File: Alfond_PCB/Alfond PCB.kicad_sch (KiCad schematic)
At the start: 33 parts, among them J1 USB_B_Micro, J2 Micro_SD_Card, U1 AMS1117-3.3, U2 DS18B20, U3 AM2302, U4 STM32U535VCT6, Y1 16MHz

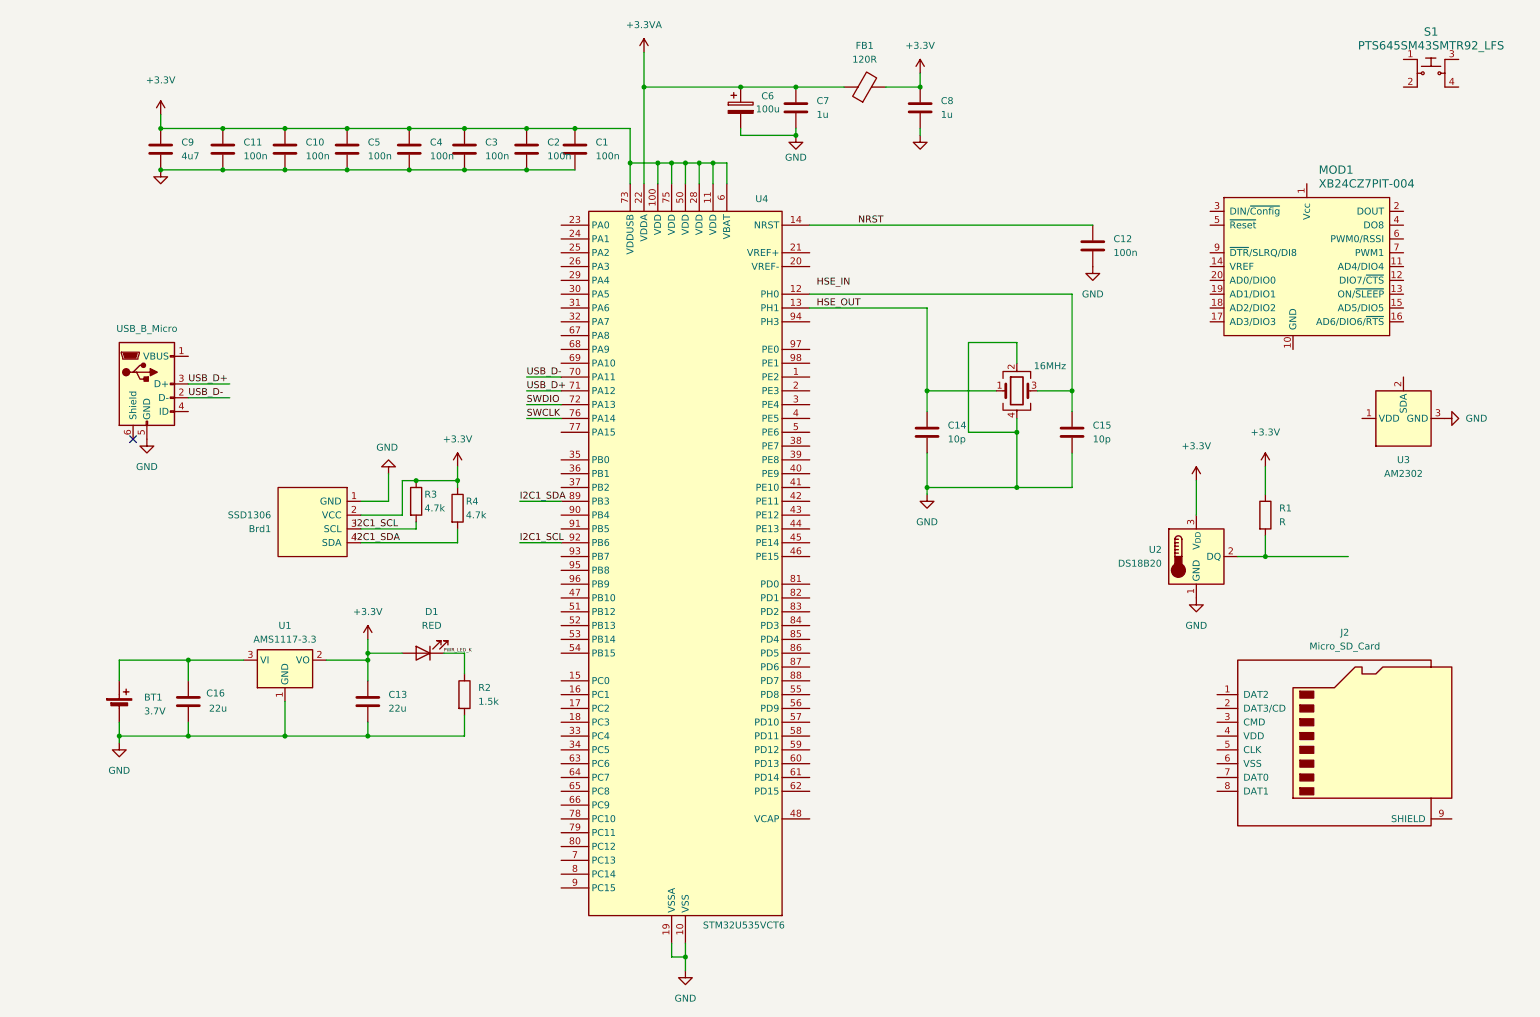
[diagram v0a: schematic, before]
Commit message: Removed stm32ide files because they were causing errors
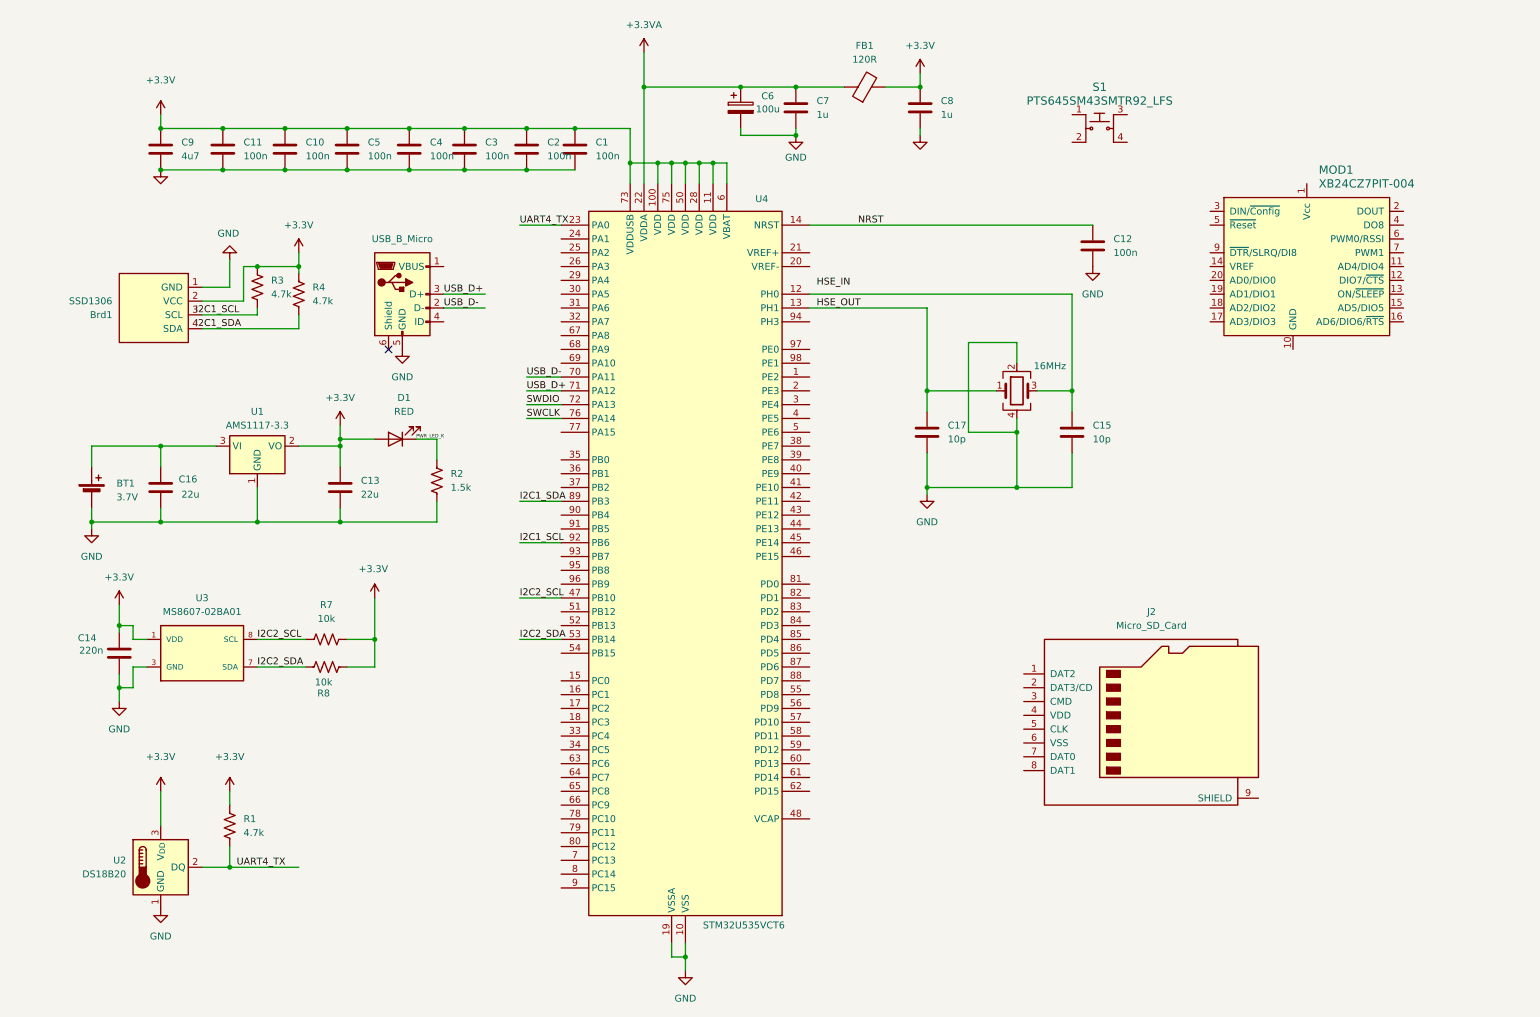
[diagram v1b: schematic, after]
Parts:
- removed R1: R, symbol Device:R
- removed R2: 1.5k, symbol Device:R
- removed R3, R4: 4.7k, symbol Device:R
- removed U3: AM2302, Sensor:ASAIR_AM2302_P2.54mm_Vertical, symbol Sensor:AM2302
- added C17: 10p, symbol Device:C
- added R1, R3, R4: 4.7k, symbol Device:R_US
- added R2: 1.5k, symbol Device:R_US
- added R7, R8: 10k, symbol Device:R_US
- added U3: MS8607-02BA01, MS8607-02BA01:MS8607-02BA01, symbol MS8607-02BA01:MS8607-02BA01
- C14: value 10p -> 220n
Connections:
- net +3.3V: now also C14.1, R1.1, R3.1, R4.1, R7.2, R8.2, U3.1 (VDD)
- net GND: now also C17.2, R2.2, U3.3 (GND)
- net HSE_OUT: now also C17.1; no longer C14.1
- net PWR_LED_K: now also R2.1
- net UART4_TX: now reaches U2.2 (DQ)
- net UART4_TX: now also U4.23 (PA0), R1.2
- net at Brd1.4 (SDA): now also R4.2
- net at Brd1.3 (SCL): now also R3.2
- net I2C2_SCL: now reaches U4.47 (PB10)
- net I2C2_SCL: now also R7.1, U3.8 (SCL)
- net I2C2_SDA: now reaches U4.53 (PB14)
- net I2C2_SDA: now also R8.1, U3.7 (SDA)
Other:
- moved on the sheet: BT1, Brd1, C13, C16, D1, J2, S1, U1, U2

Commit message: removed stm32ide files
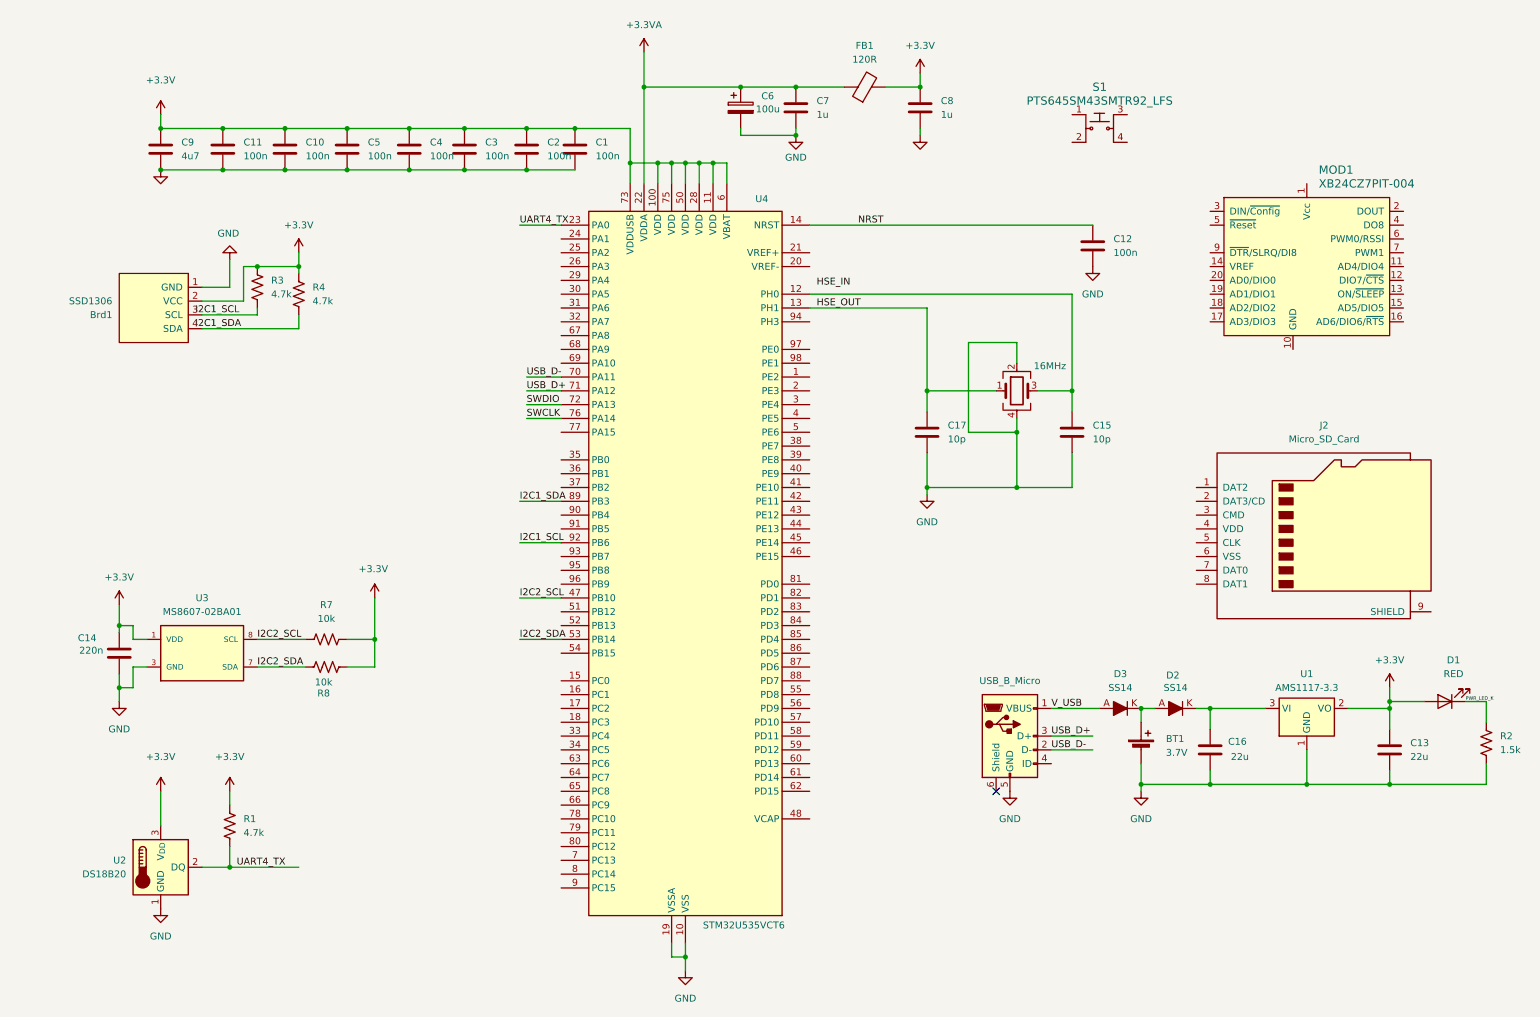
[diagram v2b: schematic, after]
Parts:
- added D2, D3: SS14, digikey-footprints:DO-214AC, symbol dk_Diodes-Rectifiers-Single:SS14
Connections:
- net V_USB: now reaches J1.1 (VBUS)
- net V_USB: now also D3.A
- net at C16.1, U1.3 (VI): now also D2.K; no longer BT1.1 (+)
- new net: BT1.1 (+), D2.A, D3.K
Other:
- moved on the sheet: BT1, C13, C16, D1, J2, R2, U1

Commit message: Updated schematic with xbee, sd card slot and button
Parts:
- removed J2: Micro_SD_Card, symbol Connector:Micro_SD_Card
- removed S1: PTS645SM43SMTR92_LFS, digikey-footprints:Switch_Tactile_SMD_6x6mm_PTS645, symbol dk_Tactile-Switches:PTS645SM43SMTR92_LFS
- added C18: 0.1u, symbol Device:C
- added D4: RED, symbol Device:LED
- added J3: Micro_SD_Card_Det_Hirose_DM3AT, symbol Connector:Micro_SD_Card_Det_Hirose_DM3AT
- added R5: 1.5k, symbol Device:R_US
- added R6: 1k, symbol Device:R_US
- added R9: 10k, symbol Device:R_US
- added S2: PTS645SM43SMTR92_LFS, digikey-footprints:Switch_Tactile_SMD_6x6mm_PTS645, symbol dk_Tactile-Switches:PTS645SM43SMTR92_LFS
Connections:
- net +3.3VA is gone; now on net +3.3V: C6.1, C7.1, FB1.1, U4.22 (VDDA)
- net +3.3V: now also MOD1.1 (Vcc), J3.4 (VDD), R9.1
- net GND: now also C1.2, C10.2, C11.2, C2.2, C3.2, C4.2, C5.2, C9.2, MOD1.10 (GND), C18.2, J3.11 (SHIELD), J3.6 (VSS), R5.2, S2.1, S2.2
- net HSE_IN: now also C15.1, U4.12 (PH0), Y1.3
- net I2C1_SCL: now also Brd1.3 (SCL), R3.2
- net I2C1_SDA: now also Brd1.4 (SDA), R4.2
- net PWR_LED_K: now also D4.1 (K), R5.1
- net at MOD1.13 (ON/~{SLEEP}): now also D4.2 (A)
- net UART5_RX: now reaches MOD1.2 (DOUT)
- net UART5_RX: now also U4.83 (PD2)
- net UART5_TX: now reaches MOD1.3 (DIN/~{Config})
- net UART5_TX: now also U4.80 (PC12)
- net GPIO_SLEEP_XBEE: now reaches MOD1.9 (~{DTR}/SLRQ/DI8)
- net GPIO_SLEEP_XBEE: now also U4.82 (PD1)
- net SPI2_MOSI: now reaches U4.16 (PC1)
- net SPI2_MOSI: now also J3.3 (CMD)
- net SPI2_MISO: now reaches U4.17 (PC2)
- net SPI2_MISO: now also J3.7 (DAT0)
- net SPI2_SCK: now reaches U4.52 (PB13)
- net SPI2_SCK: now also J3.5 (CLK)
- net GPIO_SPI_CS: now reaches U4.69 (PA10)
- net GPIO_SPI_CS: now also J3.2 (DAT3/CD)
- new net: R6.1, S2.3, S2.4
- new net GPIO_INPUT_Button: C18.1, R6.2, R9.2
- no-connect marks 1 -> 88
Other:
- moved on the sheet: BT1, C12, C13, C14, C16, D1, D2, D3, MOD1, R1, R2, R7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

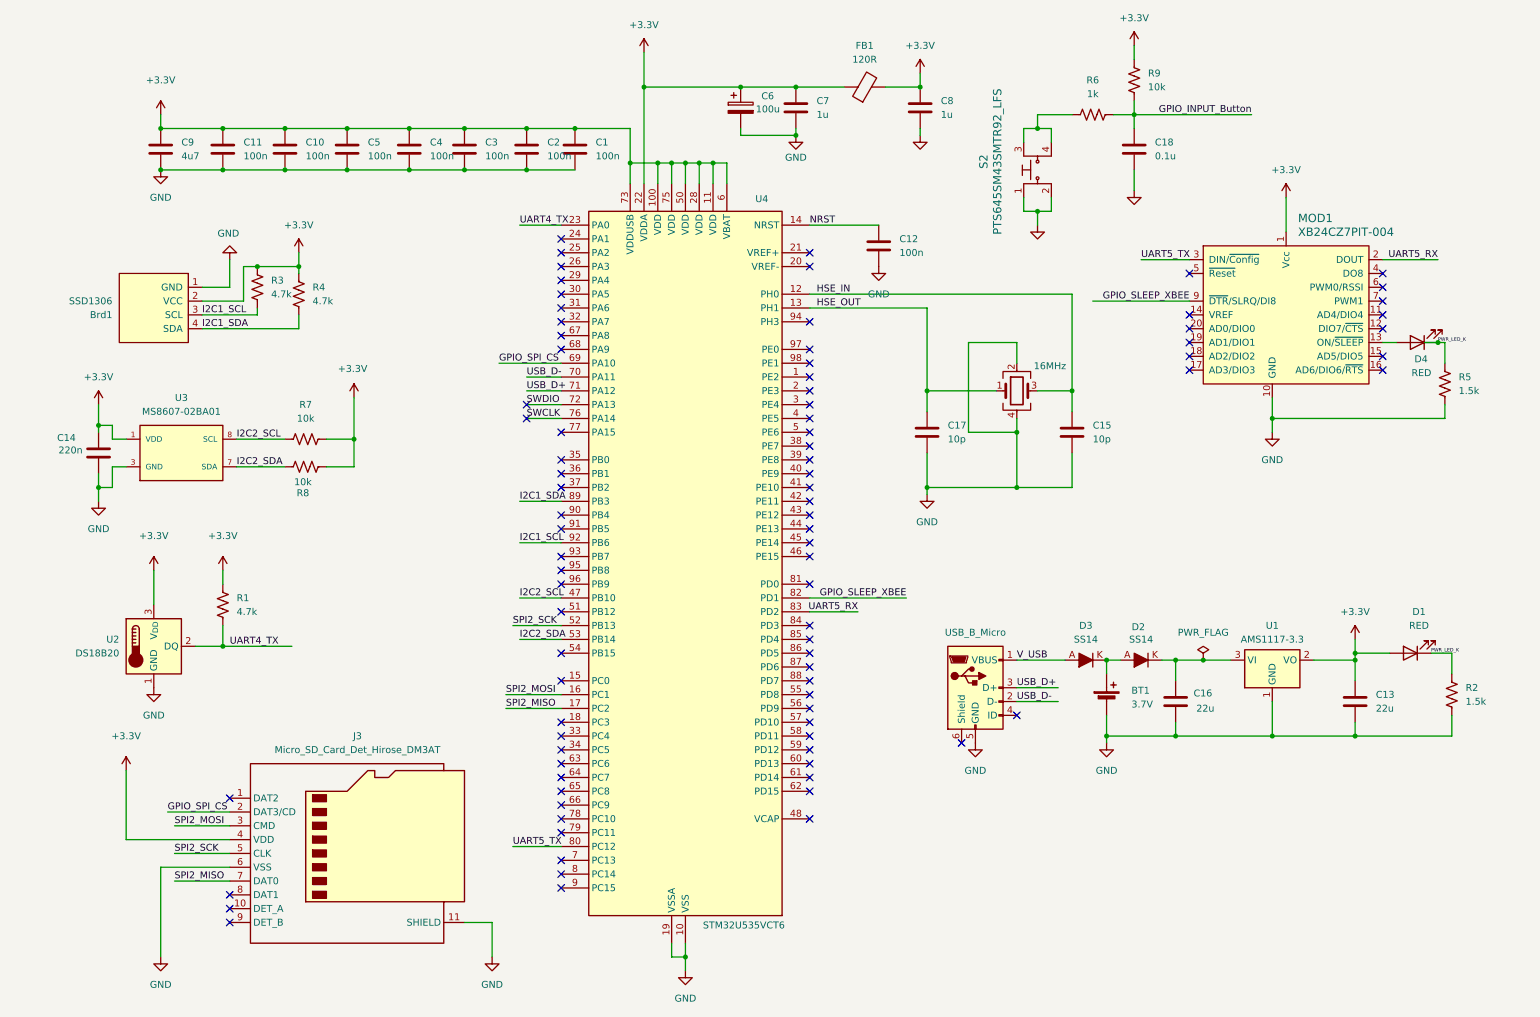
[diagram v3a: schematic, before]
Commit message: added footprints to the symbols
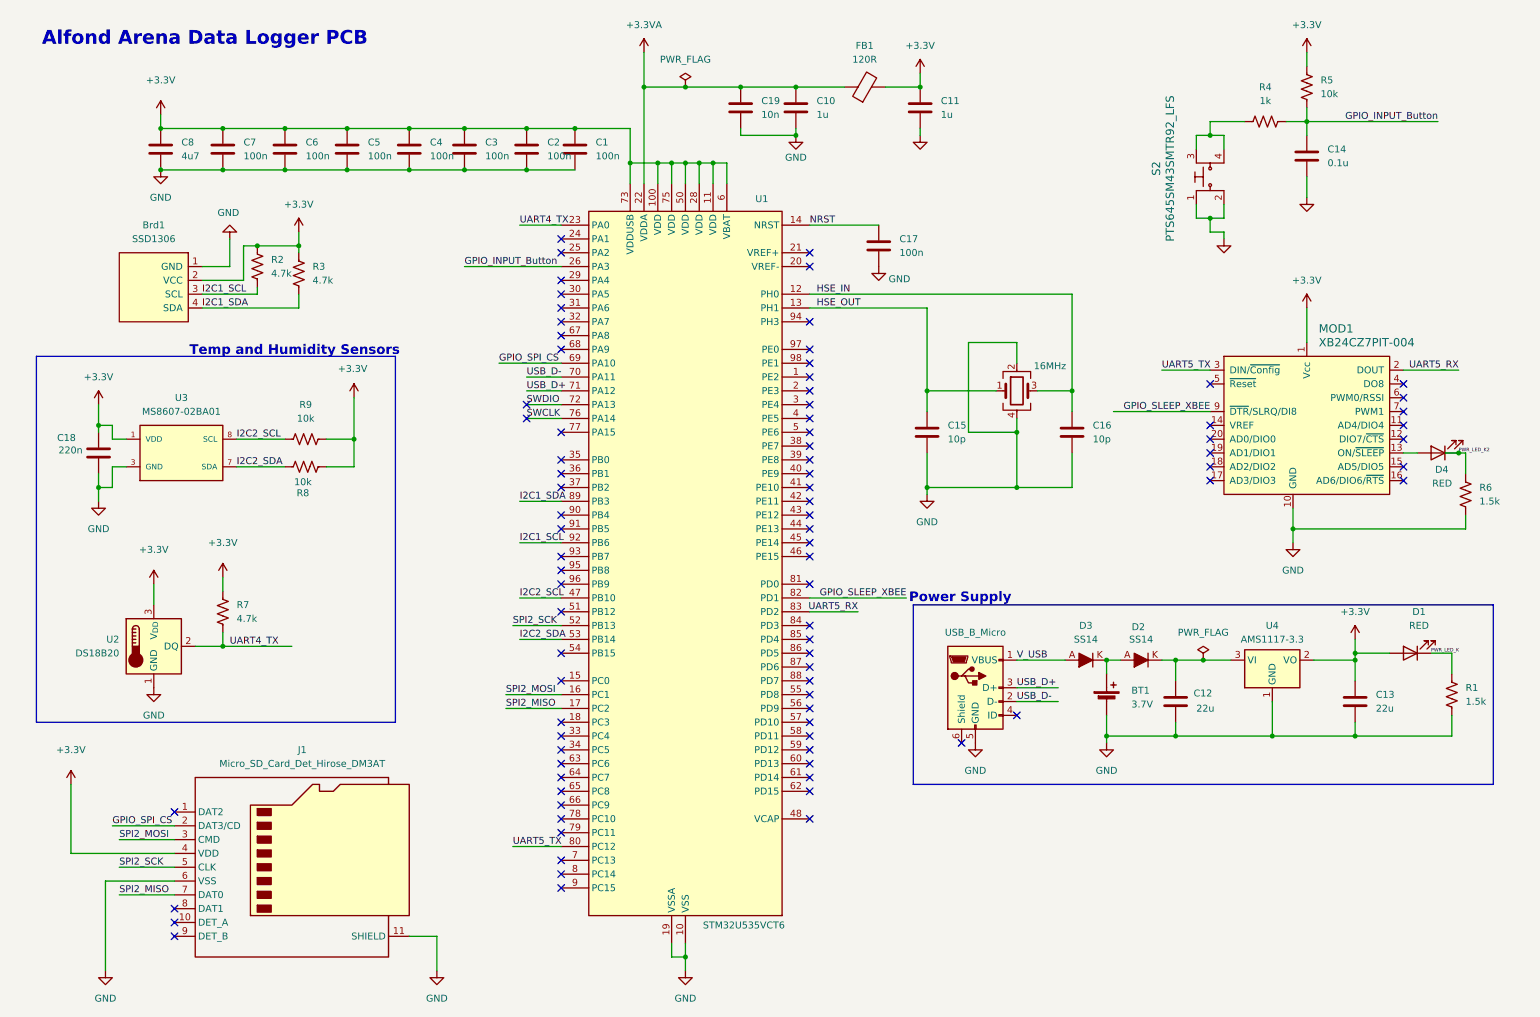
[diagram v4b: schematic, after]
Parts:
- removed C6: 100u, symbol Device:C_Polarized
- added C19: 10n, Capacitor_SMD:C_0402_1005Metric, symbol Device:C
- Brd1: footprint (none) -> SSD1306:128x64OLED
- C1, C2, C3, C4, C5: footprint (none) -> Capacitor_SMD:C_0402_1005Metric
- C10: renamed from C7; footprint (none) -> Capacitor_SMD:C_0402_1005Metric
- C11: renamed from C8; footprint (none) -> Capacitor_SMD:C_0402_1005Metric
- C12: renamed from C16; footprint (none) -> Capacitor_SMD:C_0805_2012Metric
- C13: footprint (none) -> Capacitor_SMD:C_0805_2012Metric
- C14: renamed from C18; footprint (none) -> Capacitor_SMD:C_01005_0402Metric
- C15: renamed from C17; footprint (none) -> Capacitor_SMD:C_0402_1005Metric
- C16: renamed from C15; footprint (none) -> Capacitor_SMD:C_0402_1005Metric
- C17: renamed from C12; footprint (none) -> Capacitor_SMD:C_0402_1005Metric
- C18: renamed from C14; footprint (none) -> Capacitor_SMD:C_0402_1005Metric
- C6: renamed from C10; footprint (none) -> Capacitor_SMD:C_0402_1005Metric
- C7: renamed from C11; footprint (none) -> Capacitor_SMD:C_0402_1005Metric
- C8: renamed from C9; footprint (none) -> Capacitor_SMD:C_0603_1608Metric
- D1: footprint (none) -> LED_SMD:LED_0603_1608Metric
- D4: footprint (none) -> LED_SMD:LED_0805_2012Metric
- FB1: footprint (none) -> Inductor_SMD:L_0603_1608Metric
- J1: renamed from J3; footprint (none) -> Connector_Card:microSD_HC_Hirose_DM3AT-SF-PEJM5
- J2: renamed from J1; footprint (none) -> Connector_USB:USB_Micro-B_Wuerth_629105150521
- R1: renamed from R2; footprint (none) -> Resistor_SMD:R_0402_1005Metric
- R2: renamed from R3; footprint (none) -> Resistor_SMD:R_0402_1005Metric
- R3: renamed from R4; footprint (none) -> Resistor_SMD:R_0402_1005Metric
- R4: renamed from R6; footprint (none) -> Resistor_SMD:R_0402_1005Metric
- R5: renamed from R9; footprint (none) -> Resistor_SMD:R_0402_1005Metric
- R6: renamed from R5; footprint (none) -> Resistor_SMD:R_0402_1005Metric
- R7: renamed from R1; footprint (none) -> Resistor_SMD:R_0402_1005Metric
- R8: footprint (none) -> Resistor_SMD:R_0402_1005Metric
- R9: renamed from R7; footprint (none) -> Resistor_SMD:R_0402_1005Metric
- Y1: footprint (none) -> Crystal:Crystal_SMD_3225-4Pin_3.2x2.5mm
- renumbered U4 to U1, U1 to U4
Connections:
- net +3.3V: no longer C10.1, FB1.1, U1.22 (VDDA)
- net GND: now also C19.2
- net GPIO_INPUT_Button: now also U1.26 (PA3)
- net PWR_LED_K: no longer D4.1 (K), R6.1
- new net +3.3VA: C10.1, C19.1, FB1.1, U1.22 (VDDA)
- new net PWR_LED_K2: D4.1 (K), R6.1
- no-connect marks 88 -> 87
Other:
- note added: "Alfond Arena Data Logger PCB"
- note added: "Power Supply"
- note added: "Temp and Humidity Sensors"
- title: (none) -> Alfond Arena Data Logger PCB
- moved on the sheet: Brd1, C14, D4, J1, MOD1, R2, R3, R4, R5, R6, R7, S2
